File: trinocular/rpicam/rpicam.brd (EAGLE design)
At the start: 90 x 90 mm, 9 parts, among them IC1 MEGA8-AI

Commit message: 03-12-13 20:52
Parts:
- added LEDD#1, LEDD#2: (no value), con-lstb:MA04-1
- added SRV: power, con-molex:70543-03
- added U$3: (no value), servos:HS-35HD
- U$2: value RPICAM -> (none)
- moved C1 51.5 mm to (6.70, -0.40), flipped to the bottom, turned to 90 degrees
- moved R1 48.4 mm to (-8.60, 4.80), flipped to the bottom
- moved U$1 42.1 mm to (-8.60, 3.20), flipped to the bottom
- moved ISP 40.4 mm to (-16.1, -0.60), flipped to the bottom
- moved I2C 37.5 mm to (-5.40, 10.2), flipped to the bottom, turned to 270 degrees
- moved IC1 34.1 mm to (0.00, 0.00), flipped to the bottom
- moved U$2 24.8 mm to (0.00, 0.00)
- moved UART 19.3 mm to (2.80, 10.2), turned to 180 degrees
- moved PWR 15.1 mm to (17.8, 10.2), turned to 180 degrees
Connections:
- removed net N$3: I2C.3
- removed net N$5: I2C.4
- removed net N$9: R1.2, U$1.1
- new net SCL: I2C.2, IC1.28
- new net SDA: I2C.1, IC1.27
- net +12V: now also LEDD#1.3, LEDD#2.3
- net +5V: now also I2C.4, LEDD#1.1, LEDD#2.1, U$1.1; no longer U$1.2
- net GND: now also I2C.3, LEDD#1.4, LEDD#2.4, SRV.3
- net LED1_CTRL: now also LEDD#1.2
- net LED2_CTRL: now also LEDD#2.2
- net MOSI/SRV_CTRL: now also SRV.1
- net N$1: now also R1.2, U$1.2; no longer I2C.1
- net N$2: now also SRV.2; no longer I2C.2
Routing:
- net +5V: track 17.1 -> 72.4 mm
- net MOSI/SRV_CTRL: track 10.7 -> 42.9 mm
- net LED2_CTRL: track 0.00 -> 19.0 mm
- net SCK: track 25.0 -> 11.3 mm
- net LED1_CTRL: track 0.00 -> 9.19 mm
- net SDA: track 0.00 -> 9.08 mm
- net TXD: track 0.00 -> 8.81 mm
- net SCL: track 0.00 -> 8.34 mm
- net RST: track 14.7 -> 22.4 mm
- net RXD: track 0.00 -> 7.04 mm
- net N$4: track 0.00 -> 6.02 mm
- net N$1: track 0.00 -> 1.60 mm
- net MISO: track 15.6 -> 14.9 mm, vias 0 -> 1
- added copper zone on layer 1, net GND
- added copper zone on layer 16, net GND
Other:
- board size 90 x 90 mm -> 54 x 35 mm

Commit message: 11.12.13 18:50
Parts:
- removed LEDD#1, LEDD#2: (no value), con-lstb:MA04-1
- removed PWR: power, con-molex:70543-03
- moved SRV 31.6 mm to (15.8, -11.2), flipped to the bottom, turned to 270 degrees
- moved C1 0.40 mm to (6.30, -0.40)
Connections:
- removed net +12V: LEDD#1.3, LEDD#2.3, PWR.3
- removed net N$2: SRV.2
- net +5V: now also SRV.2; no longer LEDD#1.1, LEDD#2.1, PWR.1
- net GND: no longer LEDD#1.4, LEDD#2.4, PWR.2
- net LED1_CTRL: no longer LEDD#1.2
- net LED2_CTRL: no longer LEDD#2.2
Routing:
- net +5V: track 72.4 -> 93.6 mm
- net LED2_CTRL: track 19.0 -> 0.00 mm
- net LED1_CTRL: track 9.19 -> 0.00 mm
- net MOSI/SRV_CTRL: track 42.9 -> 39.1 mm, vias 1 -> 0

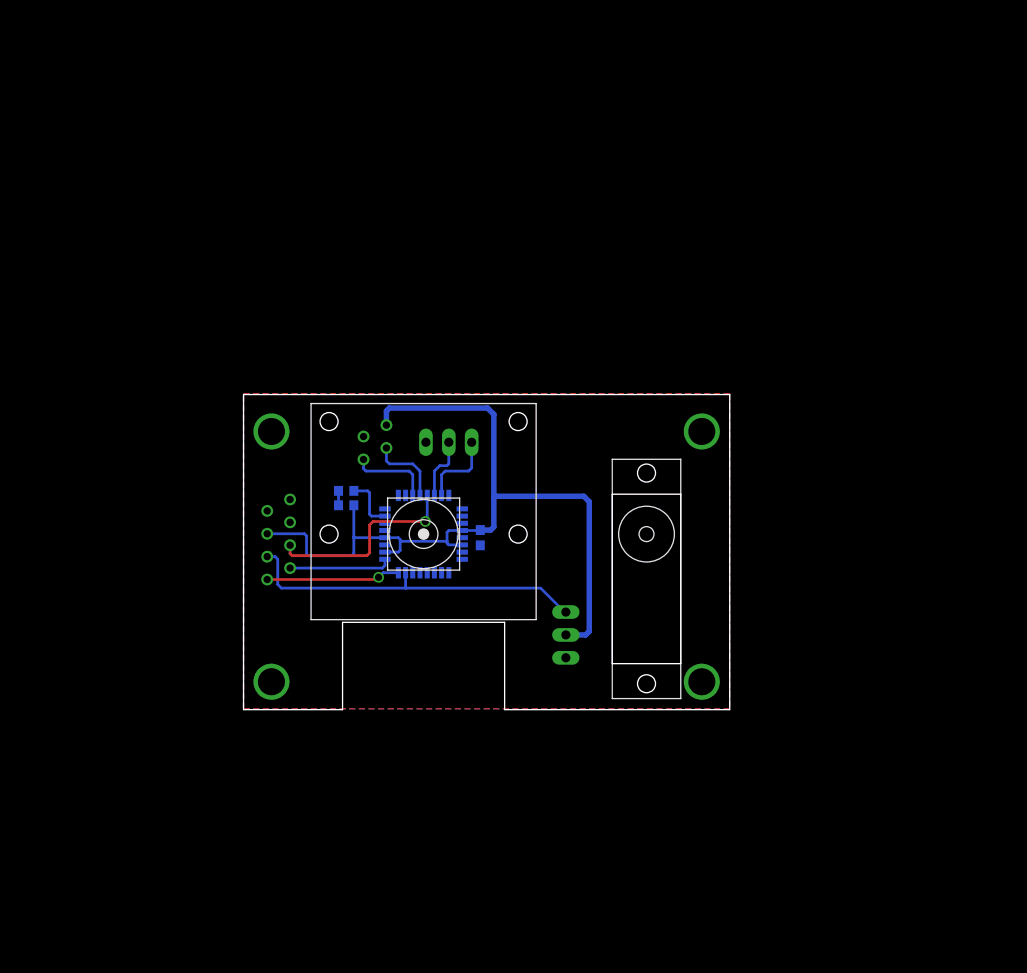
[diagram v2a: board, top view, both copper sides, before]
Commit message: trinocular: rpicam hw revisions in single files
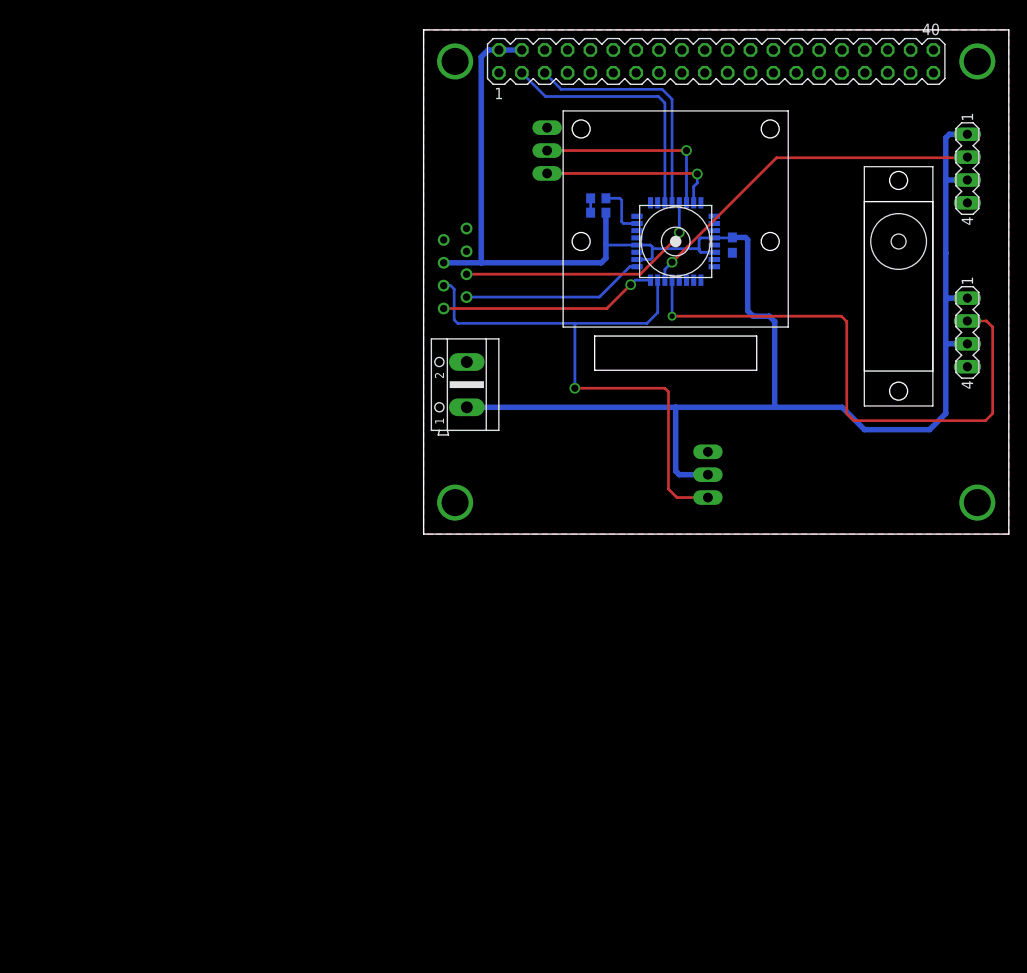
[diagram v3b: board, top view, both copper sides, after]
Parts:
- removed I2C: MICROMATCH-4, con-amp-micromatch:MICROMATCH-4
- removed SRV: power, con-molex:70543-03
- added SV1: (no value), con-lstb:MA20-2
- added SV2, SV3: (no value), con-lstb:MA04-1
- added X1: C-GRID-03-70553, con-molex:70553-03
- added X2: (no value), con-ptr500:AK500/2
- UART: device con-molex:70543-03 -> con-molex:70553-03
- moved C1 42.9 mm to (34.3, 32.1)
- moved IC1 42.9 mm to (28.0, 32.5)
- moved R1 42.9 mm to (19.4, 37.3)
- moved U$1 42.9 mm to (19.4, 35.7)
- moved U$2 42.9 mm to (28.0, 32.5)
- moved U$3 42.9 mm to (52.8, 32.5)
- moved ISP 35.9 mm to (3.50, 29.5)
- moved UART 32.6 mm to (6.10, 42.6), turned to 270 degrees
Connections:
- net +5V: now also SV1.2, SV1.4, SV2.1, SV2.3, SV3.1, SV3.3, X1.2, X2.1; no longer I2C.4, SRV.2
- net GND: now also SV1.14, SV1.20, SV1.25, SV1.30, SV1.34, SV1.39, SV1.6, SV1.9, SV2.4, SV3.4, X1.3, X2.2; no longer I2C.3, SRV.3
- net LED1_CTRL: now also SV2.2
- net LED2_CTRL: now also SV3.2
- net MOSI/SRV_CTRL: now also X1.1; no longer SRV.1
- net SCL: now also SV1.5; no longer I2C.2
- net SDA: now also SV1.3; no longer I2C.1
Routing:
- net +5V: track 93.6 -> 200.3 mm
- net LED1_CTRL: track 0.00 -> 63.4 mm, vias 0 -> 1
- net LED2_CTRL: track 0.00 -> 40.0 mm, vias 0 -> 1
- net MOSI/SRV_CTRL: track 39.1 -> 64.9 mm, vias 0 -> 1
- net SDA: track 9.08 -> 28.4 mm
- net SCL: track 8.34 -> 26.9 mm
- net RXD: track 7.04 -> 21.3 mm, vias 0 -> 1
- net TXD: track 8.81 -> 20.1 mm, vias 0 -> 1
- net MISO: track 14.9 -> 24.6 mm
- net SCK: track 11.3 -> 20.3 mm
- net RST: track 22.4 -> 29.0 mm
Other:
- board size 54 x 35 mm -> 65 x 56 mm
